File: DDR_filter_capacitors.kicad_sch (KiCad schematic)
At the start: 41 parts

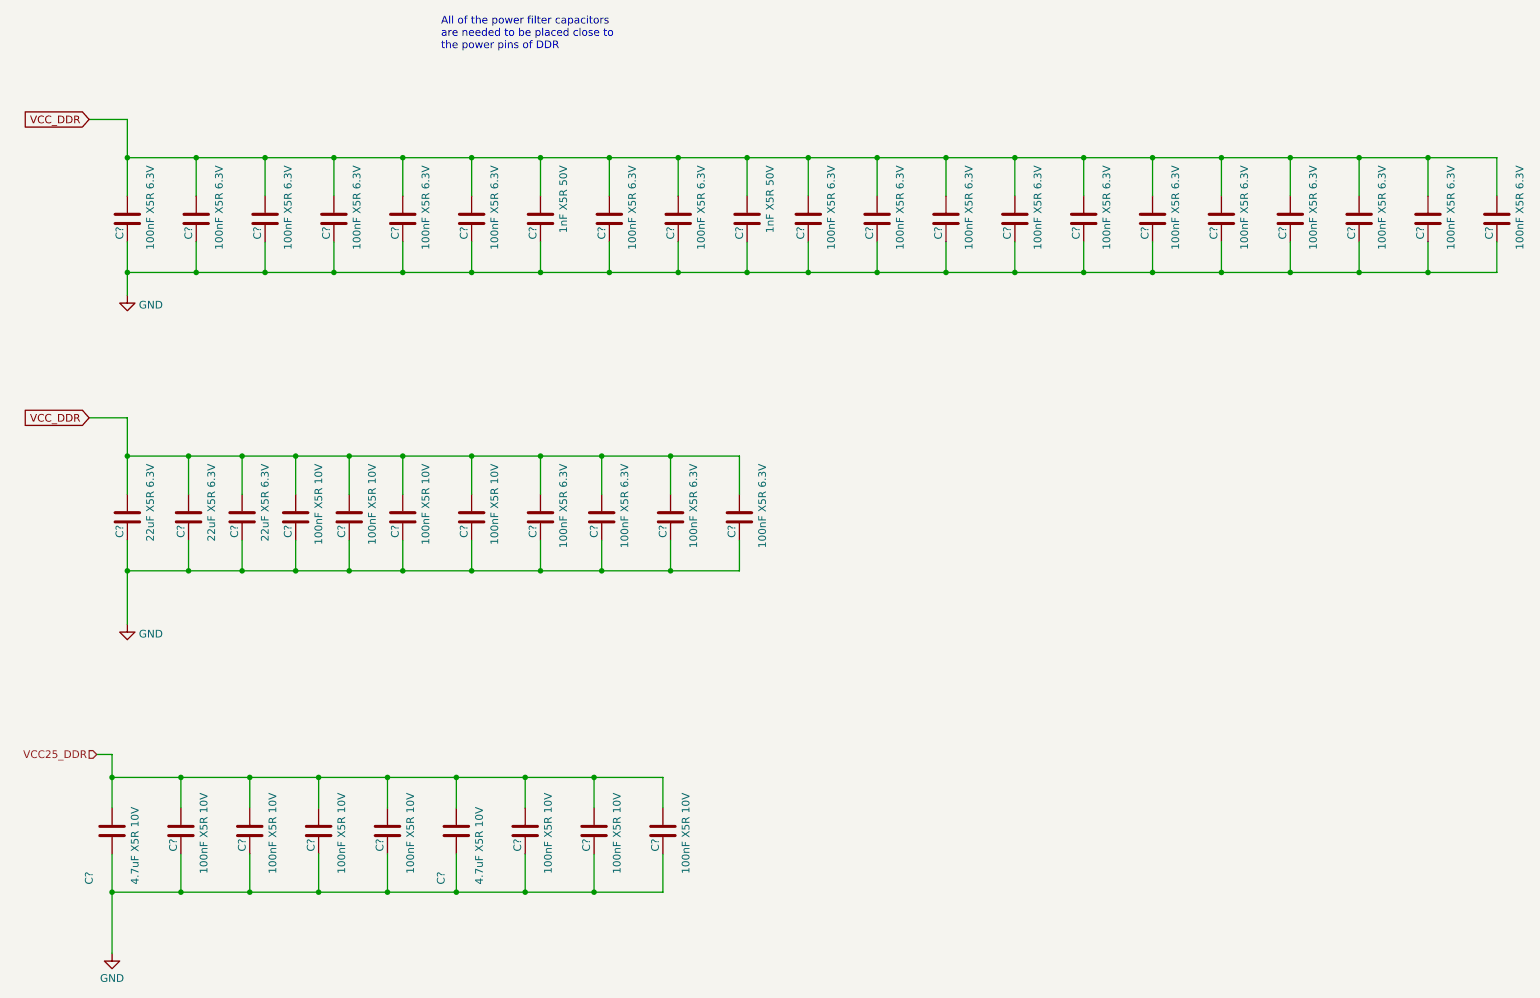
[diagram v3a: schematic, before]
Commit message: move DDR power decoupling capacitors into DDR4 Sheet
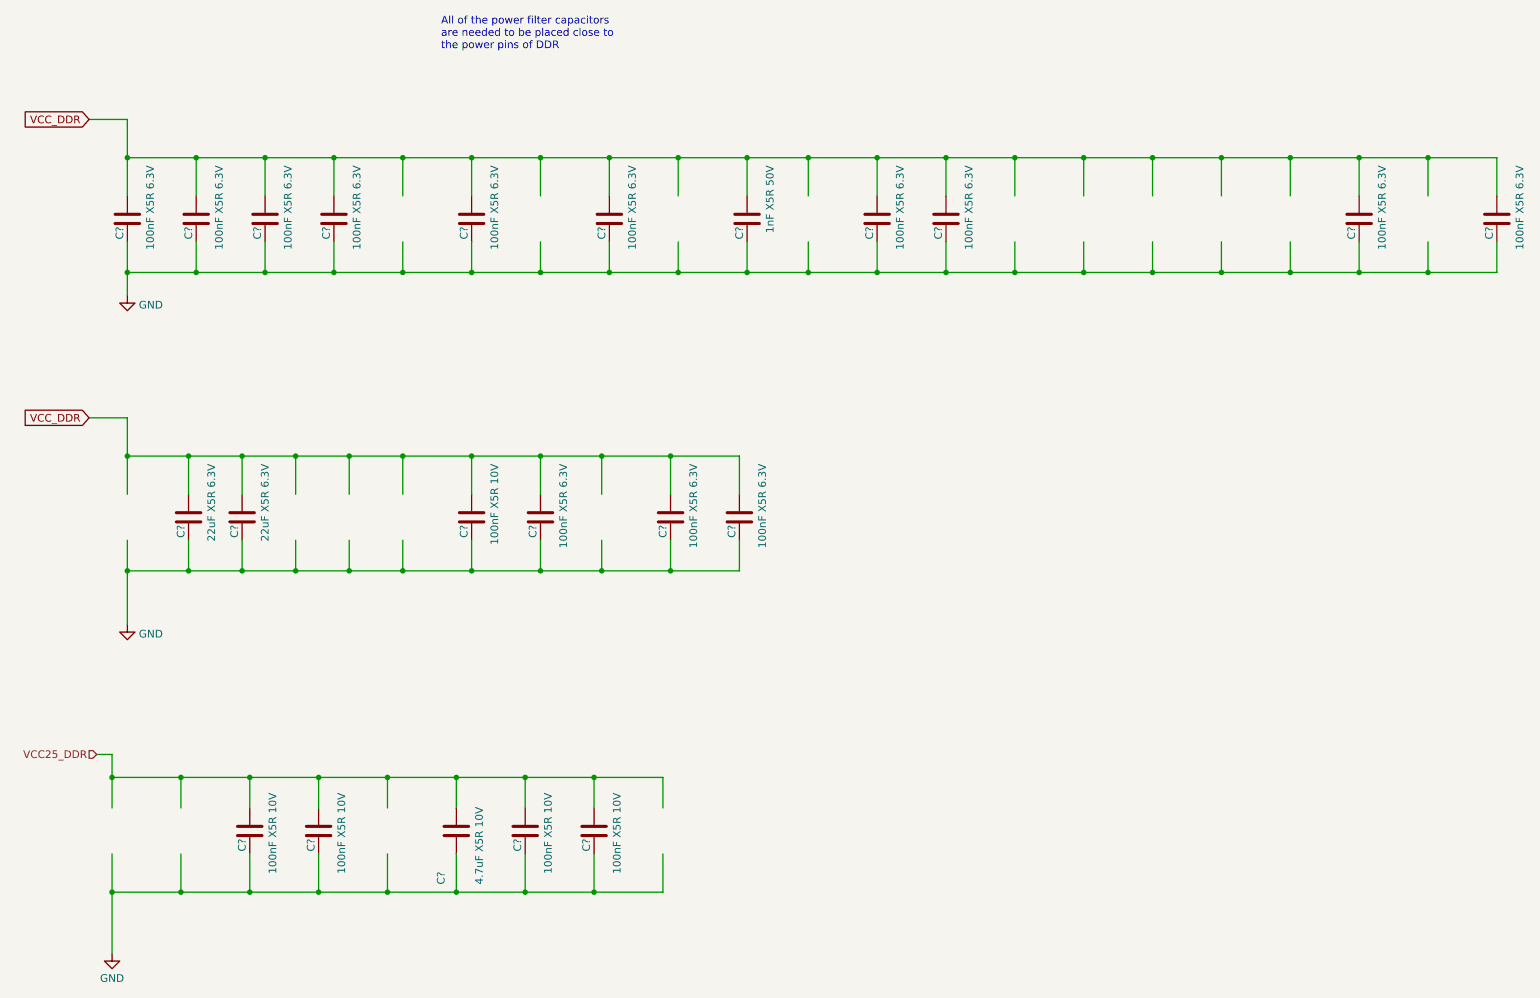
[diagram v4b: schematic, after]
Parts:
- removed C? (x10): 100nF X5R 6.3V, Capacitor_SMD:C_0201_0603Metric, symbol Device:C
- removed C?: 1nF X5R 50V, Capacitor_SMD:C_0402_1005Metric, symbol Device:C
- removed C? (x6): 100nF X5R 10V, Capacitor_SMD:C_0402_1005Metric, symbol Device:C
- removed C?: 22uF X5R 6.3V, Capacitor_SMD:C_0603_1608Metric, symbol Device:C
- removed C?: 4.7uF X5R 10V, Capacitor_SMD:C_0402_1005Metric, symbol Device:C

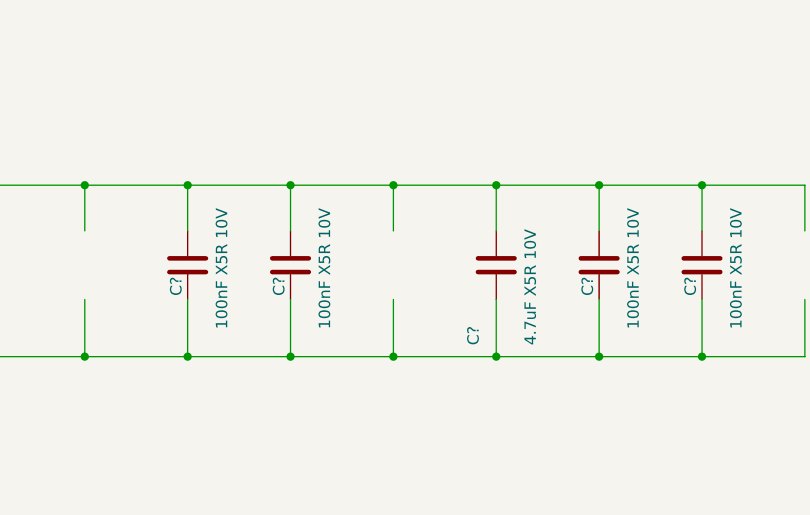
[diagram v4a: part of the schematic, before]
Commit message: added more capacitors for 2v5 output
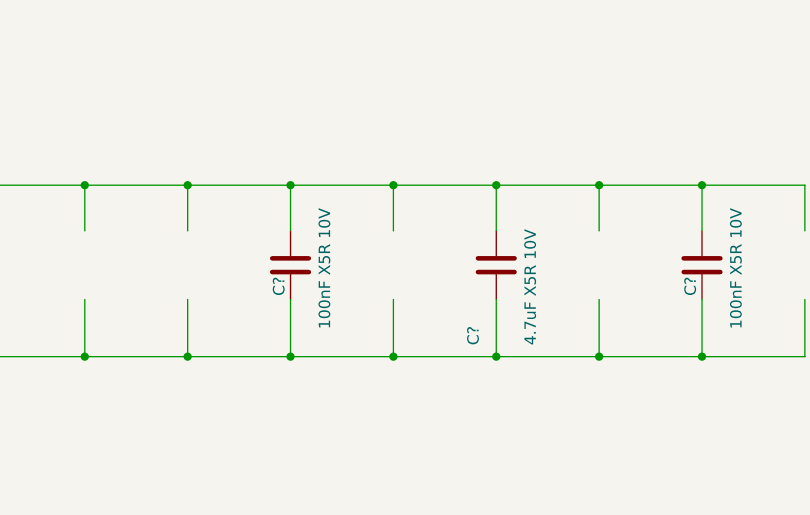
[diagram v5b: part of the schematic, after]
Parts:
- removed C? (x2): 100nF X5R 10V, Capacitor_SMD:C_0402_1005Metric, symbol Device:C
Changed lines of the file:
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@@
-    )
-  )
-  (symbol (lib_id "Device:C") (at 59.69 156.21 180) (unit 1)
-    (in_bom yes) (on_board yes) (dnp no)
-    (property "Reference" "C?" (at 58.42 157.48 90)
-      (effects (font (size 1.27 1.27)) (justify left))
-    )
-    (property "Value" "100nF X5R 10V" (at 63.5 149.86 90)
-      (effects (font (size 1.27 1.27)) (justify left))
-    )
-    (property "Footprint" "Capacitor_SMD:C_0402_1005Metric" (at 58.7248 152.4 0)
-      (effects (font (size 1.27 1.27)) hide)
-    )
-    (property "Datasheet" "~" (at 59.69 156.21 0)
-      (effects (font (size 1.27 1.27)) hide)
-    )
-    (property "Description" "容值: 100nF 精度: ±10% 额定电压: 10V 材质(温度系数): X5R 材质:X5R" (at 59.69 156.21 0)
-      (effects (font (size 1.27 1.27)) hide)
-    )
-    (property "LCSC" "C76934" (at 59.69 156.21 0)
-      (effects (font (size 1.27 1.27)) hide)
-    )
-    (property "Model" "GRM033R61A104KE15D" (at 59.69 156.21 0)
-      (effects (font (size 1.27 1.27)) hide)
-    )
-    (property "Vendor" "muRata(村田)" (at 59.69 156.21 0)
-      (effects (font (size 1.27 1.27)) hide)
-    )
-    (pin "1")
-    (pin "2")
-    (instances
-      (project "leaf"
-        (path "/e3b58043-16a3-43c8-9fad-9c9784eebfa4/9453ad46-b3ff-4d4e-8aa6-7cc75aa0f522/f6658df5-193a-49b6-ab60-4ac3c0bbbc45"
-          (reference "C?") (unit 1)
-        )
-        (path "/e3b58043-16a3-43c8-9fad-9c9784eebfa4/9453ad46-b3ff-4d4e-8aa6-7cc75aa0f522/43b336b1-9a2a-4a37-8b6d-a408b4dd9ca2/30476355-385f-41d9-8be0-39b5df88b3ca"
-          (reference "C118") (unit 1)
-        )
-      )
     )
   )
@@
         )
       )
-    )
-  )
-  (symbol (lib_id "Device:C") (at 105.41 156.21 180) (unit 1)
-    (in_bom yes) (on_board yes) (dnp no)
-    (property "Reference" "C?" (at 104.14 157.48 90)
-      (effects (font (size 1.27 1.27)) (justify left))
-    )
-    (property "Value" "100nF X5R 10V" (at 109.22 149.86 90)
-      (effects (font (size 1.27 1.27)) (justify left))
-    )
-    (property "Footprint" "Capacitor_SMD:C_0402_1005Metric" (at 104.4448 152.4 0)
-      (effects (font (size 1.27 1.27)) hide)
-    )
-    (property "Datasheet" "~" (at 105.41 156.21 0)
-      (effects (font (size 1.27 1.27)) hide)
-    )
-    (property "Description" "容值: 100nF 精度: ±10% 额定电压: 10V 材质(温度系数): X5R 材质:X5R" (at 105.41 156.21 0)
-      (effects (font (size 1.27 1.27)) hide)
-    )
-    (property "LCSC" "C76934" (at 105.41 156.21 0)
-      (effects (font (size 1.27 1.27)) hide)
-    )
-    (property "Model" "GRM033R61A104KE15D" (at 105.41 156.21 0)
-      (effects (font (size 1.27 1.27)) hide)
-    )
-    (property "Vendor" "muRata(村田)" (at 105.41 156.21 0)
-      (effects (font (size 1.27 1.27)) hide)
-    )
-    (pin "1")
-    (pin "2")
-    (instances
-      (project "leaf"
-        (path "/e3b58043-16a3-43c8-9fad-9c9784eebfa4/9453ad46-b3ff-4d4e-8aa6-7cc75aa0f522/f6658df5-193a-49b6-ab60-4ac3c0bbbc45"
-          (reference "C?") (unit 1)
-        )
-        (path "/e3b58043-16a3-43c8-9fad-9c9784eebfa4/9453ad46-b3ff-4d4e-8aa6-7cc75aa0f522/43b336b1-9a2a-4a37-8b6d-a408b4dd9ca2/30476355-385f-41d9-8be0-39b5df88b3ca"
-          (reference "C125") (unit 1)
-        )
-      )
